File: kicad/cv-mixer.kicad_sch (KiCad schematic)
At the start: 19 parts, among them J21 Eurorack Mono Jack, J22 Eurorack Mono Jack, J23 Eurorack Mono Jack, J48 Eurorack Mono Jack, U21 TL072

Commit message: component positioning mostly done
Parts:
- C2, C66, C67, C68: footprint rumblesan-standard-parts:C_Rect_L7.0mm_W3.5mm_P5.00mm -> rumblesan-standard-parts:C_Rect_L7.0mm_W2.5mm_P5.00mm
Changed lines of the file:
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@@
     (property "Reference" "C66" (id 0) (at 143.51 58.9112 90))
     (property "Value" "22pF" (id 1) (at 143.51 61.4481 90))
-    (property "Footprint" "rumblesan-standard-parts:C_Rect_L7.0mm_W3.5mm_P5.00mm" (id 2) (at 142.24 59.055 90)
+    (property "Footprint" "rumblesan-standard-parts:C_Rect_L7.0mm_W2.5mm_P5.00mm" (id 2) (at 142.24 59.055 90)
       (effects (font (size 1.27 1.27)) hide)
     )
@@
       (effects (font (size 1.27 1.27)) (justify left))
     )
-    (property "Footprint" "rumblesan-standard-parts:C_Rect_L7.0mm_W3.5mm_P5.00mm" (id 2) (at 225.425 91.44 90)
+    (property "Footprint" "rumblesan-standard-parts:C_Rect_L7.0mm_W2.5mm_P5.00mm" (id 2) (at 225.425 91.44 90)
       (effects (font (size 1.27 1.27)) hide)
     )
@@
     (property "Reference" "C2" (id 0) (at 107.95 58.9112 90))
     (property "Value" "22pF" (id 1) (at 107.95 61.4481 90))
-    (property "Footprint" "rumblesan-standard-parts:C_Rect_L7.0mm_W3.5mm_P5.00mm" (id 2) (at 106.68 59.055 90)
+    (property "Footprint" "rumblesan-standard-parts:C_Rect_L7.0mm_W2.5mm_P5.00mm" (id 2) (at 106.68 59.055 90)
       (effects (font (size 1.27 1.27)) hide)
     )
@@
       (effects (font (size 1.27 1.27)) (justify left))
     )
-    (property "Footprint" "rumblesan-standard-parts:C_Rect_L7.0mm_W3.5mm_P5.00mm" (id 2) (at 225.425 78.74 90)
-      (effects (font (size 1.27 1.27)) hide)
-    )
+    (property "Footprint" "rumblesan-standard-parts:C_Rect_L7.0mm_W2.5mm_P5.00mm" (id 2) (at 225.425 78.74 90)
+      (effects (font (size 1.27 1.27)) hide)
+    )

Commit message: Final changes for rev01
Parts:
- removed R156: 330r, rumblesan-standard-parts:R_Axial_DIN0207_L6.3mm_D2.5mm_P10.16mm_Horizontal, symbol rumblesan-standard-parts:R
- added R66: 330r, rumblesan-standard-parts:R_Axial_DIN0207_L6.3mm_D2.5mm_P10.16mm_Horizontal, symbol rumblesan-standard-parts:R
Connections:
- net CV_MIX_OUT: now also U21.7, R66.2; no longer J48.T (Tip)
- new net: J48.T (Tip), R66.1
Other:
- moved on the sheet: C67, C68, J48, U21C

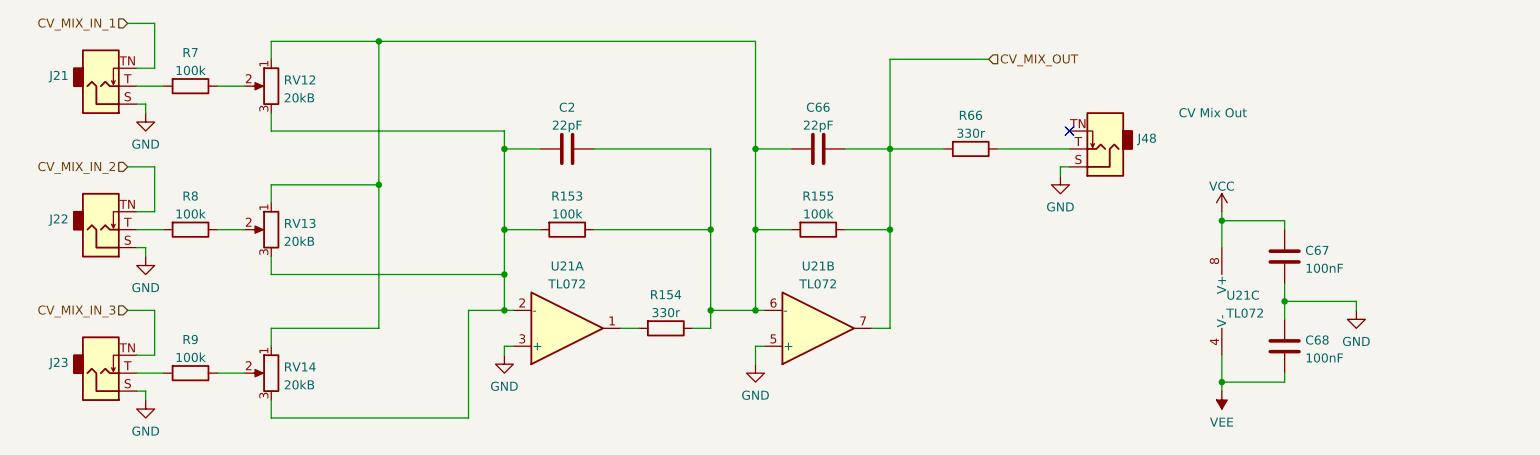
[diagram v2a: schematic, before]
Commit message: Full rejig to use attiny for divider
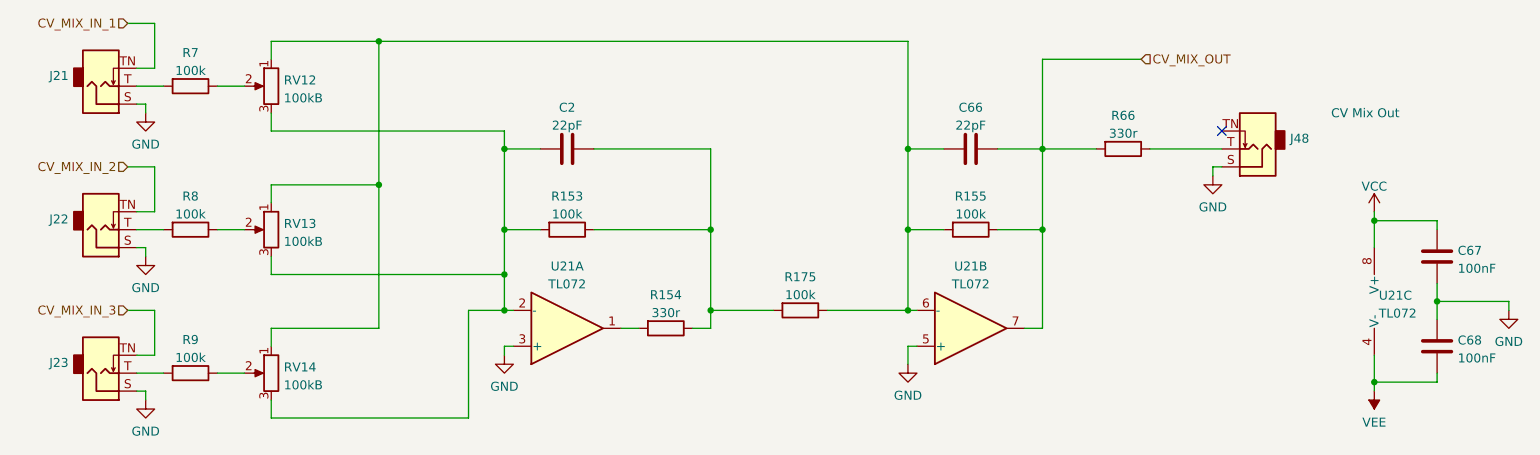
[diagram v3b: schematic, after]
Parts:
- added R175: 100k, rumblesan-standard-parts:R_Axial_DIN0207_L6.3mm_D2.5mm_P10.16mm_Horizontal, symbol rumblesan-standard-parts:R
- C67, C68: Spec ceramic C0G -> ceramic X7R
- RV12, RV13, RV14: value 20kB -> 100kB
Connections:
- net at C66.1, R155.2, RV12.1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: now also R175.1; no longer C2.2, R153.1, R154.1
- new net: C2.2, R153.1, R154.1, R175.2
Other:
- moved on the sheet: C66, C67, C68, J48, R155, R66, U21B, U21C

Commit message: Changing name to the mercurial machine
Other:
- title: (none) -> The Mercurial Machine
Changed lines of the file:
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@@
 (kicad_sch (version 20211123) (generator eeschema)
   (paper "A4")
+  (title_block
+    (title "The Mercurial Machine")
+    (date "2023-05-13")
+    (rev "r02")
+    (comment 2 "creativecommons.org/licenses/by/4.0/")
+    (comment 3 "License: CC BY 4.0")
+    (comment 4 "Author: Guy John")
+  )
   (junction (at 99.06 82.55) (diameter 0) (color 0 0 0 0)
   )

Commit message: geographically reannotate parts
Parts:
- renumbered C2 to C10, C66 to C7, C67 to C8, C68 to C9, J23 to J15, J22 to J16, J21 to J17, J48 to J18, R155 to R28, R9 to R29, R8 to R30, R7 to R31, R66 to R33, R175 to R36, R154 to R37, R153 to R38, RV14 to RV15, RV13 to RV16, RV12 to RV17, U21 to U2
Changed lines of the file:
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@@
   (symbol (lib_id "Eurorack_Hardware:Eurorack Mono Jack") (at 41.91 54.61 0) (mirror y) (unit 1)
     (in_bom yes) (on_board yes) (fields_autoplaced)
-    (property "Reference" "J21" (id 0) (at 37.338 54.4103 0)
+    (property "Reference" "J17" (id 0) (at 37.338 54.4103 0)
       (effects (font (size 1.27 1.27)) (justify left))
     )
@@
   (symbol (lib_id "rumblesan-standard-parts:R") (at 54.61 76.2 90) (unit 1)
     (in_bom yes) (on_board yes) (fields_autoplaced)
-    (property "Reference" "R8" (id 0) (at 54.61 71.4842 90))
+    (property "Reference" "R30" (id 0) (at 54.61 71.4842 90))
     (property "Value" "100k" (id 1) (at 54.61 74.0211 90))
     (property "Footprint" "rumblesan-standard-parts:R_Axial_DIN0207_L6.3mm_D2.5mm_P10.16mm_Horizontal" (id 2) (at 57.15 73.66 90)
@@
   (symbol (lib_id "Device:R_Potentiometer") (at 66.04 55.88 0) (mirror y) (unit 1)
     (in_bom yes) (on_board yes) (fields_autoplaced)
-    (property "Reference" "RV12" (id 0) (at 67.818 55.0453 0)
+    (property "Reference" "RV17" (id 0) (at 67.818 55.0453 0)
       (effects (font (size 1.27 1.27)) (justify right))
     )
@@
   (symbol (lib_id "Eurorack_Hardware:Eurorack Mono Jack") (at 205.74 63.5 0) (unit 1)
     (in_bom yes) (on_board yes)
-    (property "Reference" "J48" (id 0) (at 210.312 63.3003 0)
+    (property "Reference" "J18" (id 0) (at 210.312 63.3003 0)
       (effects (font (size 1.27 1.27)) (justify left))
     )
@@
   (symbol (lib_id "rumblesan-standard-parts:R") (at 54.61 96.52 90) (unit 1)
     (in_bom yes) (on_board yes) (fields_autoplaced)
-    (property "Reference" "R9" (id 0) (at 54.61 91.8042 90))
+    (property "Reference" "R29" (id 0) (at 54.61 91.8042 90))
     (property "Value" "100k" (id 1) (at 54.61 94.3411 90))
     (property "Footprint" "rumblesan-standard-parts:R_Axial_DIN0207_L6.3mm_D2.5mm_P10.16mm_Horizontal" (id 2) (at 57.15 93.98 90)
@@
   (symbol (lib_id "rumblesan-standard-parts:C") (at 165.1 64.77 90) (unit 1)
     (in_bom yes) (on_board yes) (fields_autoplaced)
-    (property "Reference" "C66" (id 0) (at 165.1 58.9112 90))
+    (property "Reference" "C7" (id 0) (at 165.1 58.9112 90))
     (property "Value" "22pF" (id 1) (at 165.1 61.4481 90))
     (property "Footprint" "rumblesan-standard-parts:C_Rect_L7.0mm_W2.5mm_P5.00mm" (id 2) (at 163.83 59.055 90)
@@
   (symbol (lib_id "rumblesan-standard-parts:C") (at 231.14 92.71 0) (unit 1)
     (in_bom yes) (on_board yes) (fields_autoplaced)
-    (property "Reference" "C68" (id 0) (at 234.061 91.8753 0)
+    (property "Reference" "C9" (id 0) (at 234.061 91.8753 0)
       (effects (font (size 1.27 1.27)) (justify left))
     )
@@
   (symbol (lib_id "rumblesan-standard-parts:R") (at 54.61 55.88 90) (unit 1)
     (in_bom yes) (on_board yes) (fields_autoplaced)
-    (property "Reference" "R7" (id 0) (at 54.61 51.1642 90))
+    (property "Reference" "R31" (id 0) (at 54.61 51.1642 90))
     (property "Value" "100k" (id 1) (at 54.61 53.7011 90))
     (property "Footprint" "rumblesan-standard-parts:R_Axial_DIN0207_L6.3mm_D2.5mm_P10.16mm_Horizontal" (id 2) (at 57.15 53.34 90)
@@
   (symbol (lib_id "rumblesan-standard-parts:R") (at 165.1 76.2 90) (unit 1)
     (in_bom yes) (on_board yes) (fields_autoplaced)
-    (property "Reference" "R155" (id 0) (at 165.1 71.4842 90))
+    (property "Reference" "R28" (id 0) (at 165.1 71.4842 90))
     (property "Value" "100k" (id 1) (at 165.1 74.0211 90))
     (property "Footprint" "rumblesan-standard-parts:R_Axial_DIN0207_L6.3mm_D2.5mm_P10.16mm_Horizontal" (id 2) (at 167.64 73.66 90)
@@
   (symbol (lib_id "rumblesan-standard-parts:R") (at 121.92 90.17 90) (unit 1)
     (in_bom yes) (on_board yes) (fields_autoplaced)
-    (property "Reference" "R154" (id 0) (at 121.92 85.4542 90))
+    (property "Reference" "R37" (id 0) (at 121.92 85.4542 90))
     (property "Value" "330r" (id 1) (at 121.92 87.9911 90))
     (property "Footprint" "rumblesan-standard-parts:R_Axial_DIN0207_L6.3mm_D2.5mm_P10.16mm_Horizontal" (id 2) (at 124.46 87.63 90)
@@
   (symbol (lib_id "rumblesan-standard-parts:R") (at 186.69 64.77 90) (unit 1)
     (in_bom yes) (on_board yes) (fields_autoplaced)
-    (property "Reference" "R66" (id 0) (at 186.69 60.0542 90))
+    (property "Reference" "R33" (id 0) (at 186.69 60.0542 90))
     (property "Value" "330r" (id 1) (at 186.69 62.5911 90))
     (property "Footprint" "rumblesan-standard-parts:R_Axial_DIN0207_L6.3mm_D2.5mm_P10.16mm_Horizontal" (id 2) (at 189.23 62.23 90)
@@
   (symbol (lib_id "Amplifier_Operational:TL072") (at 224.79 86.36 0) (unit 3)
     (in_bom yes) (on_board yes) (fields_autoplaced)
-    (property "Reference" "U21" (id 0) (at 222.885 85.5253 0)
+    (property "Reference" "U2" (id 0) (at 222.885 85.5253 0)
       (effects (font (size 1.27 1.27)) (justify left))
     )
@@
   (symbol (lib_id "Eurorack_Hardware:Eurorack Mono Jack") (at 41.91 95.25 0) (mirror y) (unit 1)
     (in_bom yes) (on_board yes) (fields_autoplaced)
-    (property "Reference" "J23" (id 0) (at 37.338 95.0503 0)
+    (property "Reference" "J15" (id 0) (at 37.338 95.0503 0)
       (effects (font (size 1.27 1.27)) (justify left))
     )
@@
   (symbol (lib_id "Amplifier_Operational:TL072") (at 165.1 90.17 0) (mirror x) (unit 2)
     (in_bom yes) (on_board yes) (fields_autoplaced)
-    (property "Reference" "U21" (id 0) (at 165.1 81.3902 0))
+    (property "Reference" "U2" (id 0) (at 165.1 81.3902 0))
     (property "Value" "TL072" (id 1) (at 165.1 83.9271 0))
     (property "Footprint" "rumblesan-standard-parts:DIP-8_W7.62mm_Socket" (id 2) (at 165.1 90.17 0)
@@
   (symbol (lib_id "Amplifier_Operational:TL072") (at 107.95 90.17 0) (mirror x) (unit 1)
     (in_bom yes) (on_board yes) (fields_autoplaced)
-    (property "Reference" "U21" (id 0) (at 107.95 81.3902 0))
+    (property "Reference" "U2" (id 0) (at 107.95 81.3902 0))
     (property "Value" "TL072" (id 1) (at 107.95 83.9271 0))
     (property "Footprint" "rumblesan-standard-parts:DIP-8_W7.62mm_Socket" (id 2) (at 107.95 90.17 0)
@@
   (symbol (lib_id "rumblesan-standard-parts:R") (at 107.95 76.2 90) (unit 1)
     (in_bom yes) (on_board yes) (fields_autoplaced)
-    (property "Reference" "R153" (id 0) (at 107.95 71.4842 90))
+    (property "Reference" "R38" (id 0) (at 107.95 71.4842 90))
     (property "Value" "100k" (id 1) (at 107.95 74.0211 90))
     (property "Footprint" "rumblesan-standard-parts:R_Axial_DIN0207_L6.3mm_D2.5mm_P10.16mm_Horizontal" (id 2) (at 110.49 73.66 90)
@@
   (symbol (lib_id "Eurorack_Hardware:Eurorack Mono Jack") (at 41.91 74.93 0) (mirror y) (unit 1)
     (in_bom yes) (on_board yes) (fields_autoplaced)
-    (property "Reference" "J22" (id 0) (at 37.338 74.7303 0)
+    (property "Reference" "J16" (id 0) (at 37.338 74.7303 0)
       (effects (font (size 1.27 1.27)) (justify left))
     )
@@
   (symbol (lib_id "rumblesan-standard-parts:R") (at 140.97 87.63 90) (unit 1)
     (in_bom yes) (on_board yes) (fields_autoplaced)
-    (property "Reference" "R175" (id 0) (at 140.97 82.9142 90))
+    (property "Reference" "R36" (id 0) (at 140.97 82.9142 90))
     (property "Value" "100k" (id 1) (at 140.97 85.4511 90))
     (property "Footprint" "rumblesan-standard-parts:R_Axial_DIN0207_L6.3mm_D2.5mm_P10.16mm_Horizontal" (id 2) (at 143.51 85.09 90)
@@
   (symbol (lib_id "Device:R_Potentiometer") (at 66.04 76.2 0) (mirror y) (unit 1)
     (in_bom yes) (on_board yes) (fields_autoplaced)
-    (property "Reference" "RV13" (id 0) (at 67.818 75.3653 0)
+    (property "Reference" "RV16" (id 0) (at 67.818 75.3653 0)
       (effects (font (size 1.27 1.27)) (justify right))
     )
@@
   (symbol (lib_id "rumblesan-standard-parts:C") (at 107.95 64.77 90) (unit 1)
     (in_bom yes) (on_board yes) (fields_autoplaced)
-    (property "Reference" "C2" (id 0) (at 107.95 58.9112 90))
+    (property "Reference" "C10" (id 0) (at 107.95 58.9112 90))
     (property "Value" "22pF" (id 1) (at 107.95 61.4481 90))
     (property "Footprint" "rumblesan-standard-parts:C_Rect_L7.0mm_W2.5mm_P5.00mm" (id 2) (at 106.68 59.055 90)
@@
   (symbol (lib_id "Device:R_Potentiometer") (at 66.04 96.52 0) (mirror y) (unit 1)
     (in_bom yes) (on_board yes) (fields_autoplaced)
-    (property "Reference" "RV14" (id 0) (at 67.818 95.6853 0)
+    (property "Reference" "RV15" (id 0) (at 67.818 95.6853 0)
       (effects (font (size 1.27 1.27)) (justify right))
     )
@@
   (symbol (lib_id "rumblesan-standard-parts:C") (at 231.14 80.01 0) (unit 1)
     (in_bom yes) (on_board yes) (fields_autoplaced)
-    (property "Reference" "C67" (id 0) (at 234.061 79.1753 0)
-      (effects (font (size 1.27 1.27)) (justify left))
-    )
+    (property "Reference" "C8" (id 0) (at 234.061 79.1753 0)
+      (effects (font (size 1.27 1.27)) (justify left))
+    )

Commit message: Changing name again
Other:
- title: The Mercurial Machine -> Ouroboros
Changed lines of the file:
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@@
   (paper "A4")
   (title_block
-    (title "The Mercurial Machine")
+    (title "Ouroboros")
     (date "2023-05-13")
     (rev "r02")

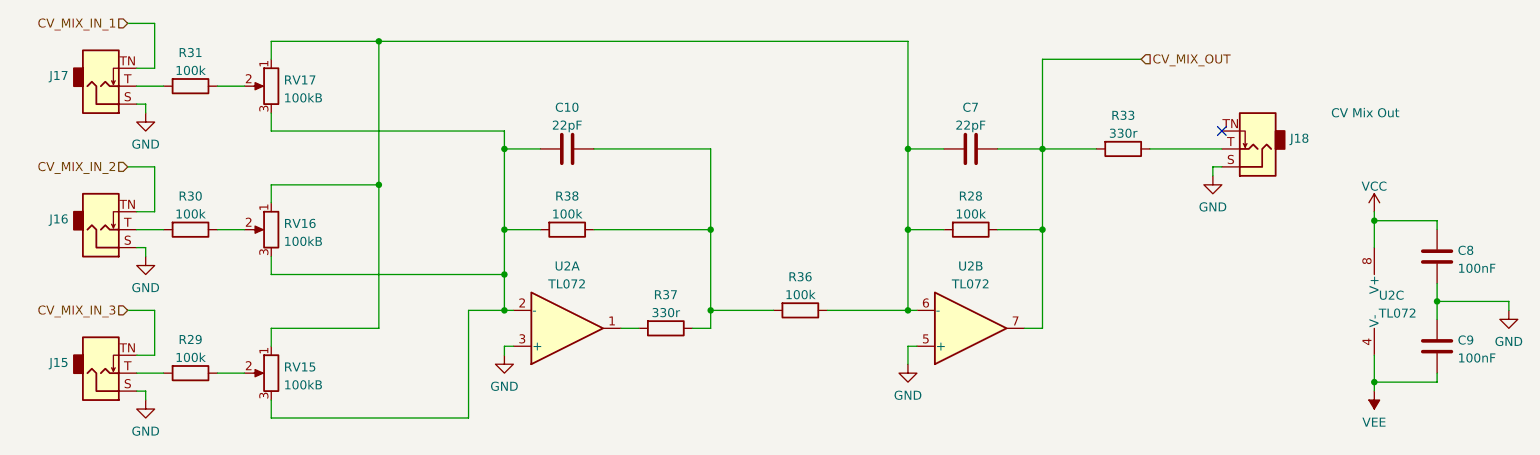
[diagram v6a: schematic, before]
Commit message: Updating for kicad 7
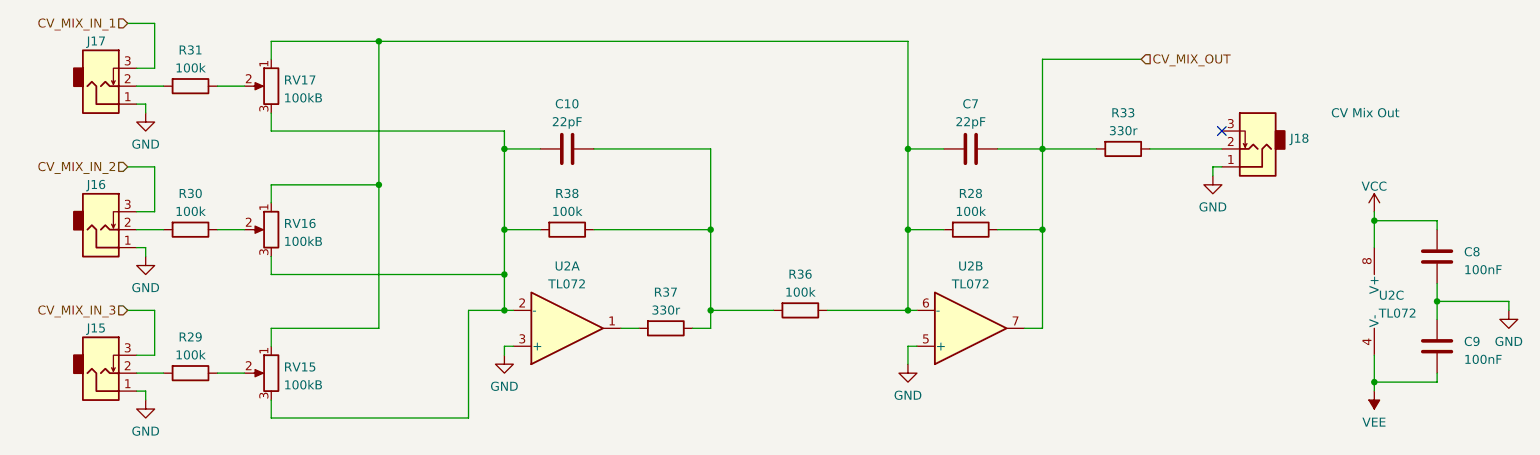
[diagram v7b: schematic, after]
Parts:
- C10, C7: footprint rumblesan-standard-parts:C_Rect_L7.0mm_W2.5mm_P5.00mm -> Rumblesan_Standard_Parts:C_Rect_L7.0mm_W2.5mm_P5.00mm; symbol rumblesan-standard-parts:C -> Rumblesan Standard Parts:C
- C8, C9: footprint rumblesan-standard-parts:C_Rect_L7.0mm_W2.5mm_P5.00mm -> Rumblesan_Standard_Parts:C_Rect_L7.0mm_W2.5mm_P5.00mm; symbol rumblesan-standard-parts:C -> Rumblesan Standard Parts:C; Spec ceramic X7R -> ceramic C0G
- J15, J16, J17, J18: footprint rumblesan-standard-parts:Jack_3.5mm_QingPu_WQP-PJ398SM_Vertical -> Rumblesan_Standard_Parts:Jack_3.5mm_QingPu_WQP-PJ398SM_Vertical; symbol Eurorack_Hardware:Eurorack Mono Jack -> Audio_Connectors:Eurorack_Mono_Jack
- R28, R29, R30, R31, R33, R36, R37, R38: footprint rumblesan-standard-parts:R_Axial_DIN0207_L6.3mm_D2.5mm_P10.16mm_Horizontal -> Rumblesan_Standard_Parts:R_Axial_DIN0207_L6.3mm_D2.5mm_P10.16mm_Horizontal; symbol rumblesan-standard-parts:R -> Rumblesan Standard Parts:R
- RV15, RV16, RV17: footprint rumblesan-standard-parts:Potentiometer_Alpha_RD901F-40-00D_Single_Vertical -> Rumblesan_Standard_Parts:Potentiometer_Alpha_RD901F-40-00D_Single_Vertical; symbol Device:R_Potentiometer -> Rumblesan Standard Parts:R_Potentiometer
- U2: footprint rumblesan-standard-parts:DIP-8_W7.62mm_Socket -> Rumblesan_Standard_Parts:DIP-8_W7.62mm_Socket
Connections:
- net CV_MIX_IN_1: now also J17.3 (Tip_normalize); no longer J17.TN (Tip_normalize)
- net CV_MIX_IN_2: now also J16.3 (Tip_normalize); no longer J16.TN (Tip_normalize)
- net CV_MIX_IN_3: now also J15.3 (Tip_normalize); no longer J15.TN (Tip_normalize)
- net GND: now also J15.1 (Sleeve), J16.1 (Sleeve), J17.1 (Sleeve), J18.1 (Sleeve); no longer J15.S (Sleeve), J16.S (Sleeve), J17.S (Sleeve), J18.S (Sleeve)
- net at R31.2: now also J17.2 (Tip); no longer J17.T (Tip)
- net at R30.2: now also J16.2 (Tip); no longer J16.T (Tip)
- net at R33.1: now also J18.2 (Tip); no longer J18.T (Tip)
- net at R29.2: now also J15.2 (Tip); no longer J15.T (Tip)

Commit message: Changing decoupling caps to ceramic X7R
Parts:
- C8, C9: Spec ceramic C0G -> ceramic X7R
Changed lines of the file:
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@@
       (effects (font (size 1.27 1.27)) hide)
     )
-    (property "Spec" "ceramic C0G" (at 234.95 92.71 90)
+    (property "Spec" "ceramic X7R" (at 234.95 92.71 90)
       (effects (font (size 1.27 1.27)) hide)
     )
@@
       (effects (font (size 1.27 1.27)) hide)
     )
-    (property "Spec" "ceramic C0G" (at 234.95 80.01 90)
-      (effects (font (size 1.27 1.27)) hide)
-    )
+    (property "Spec" "ceramic X7R" (at 234.95 80.01 90)
+      (effects (font (size 1.27 1.27)) hide)
+    )
